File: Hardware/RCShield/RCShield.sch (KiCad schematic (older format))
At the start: 34 parts

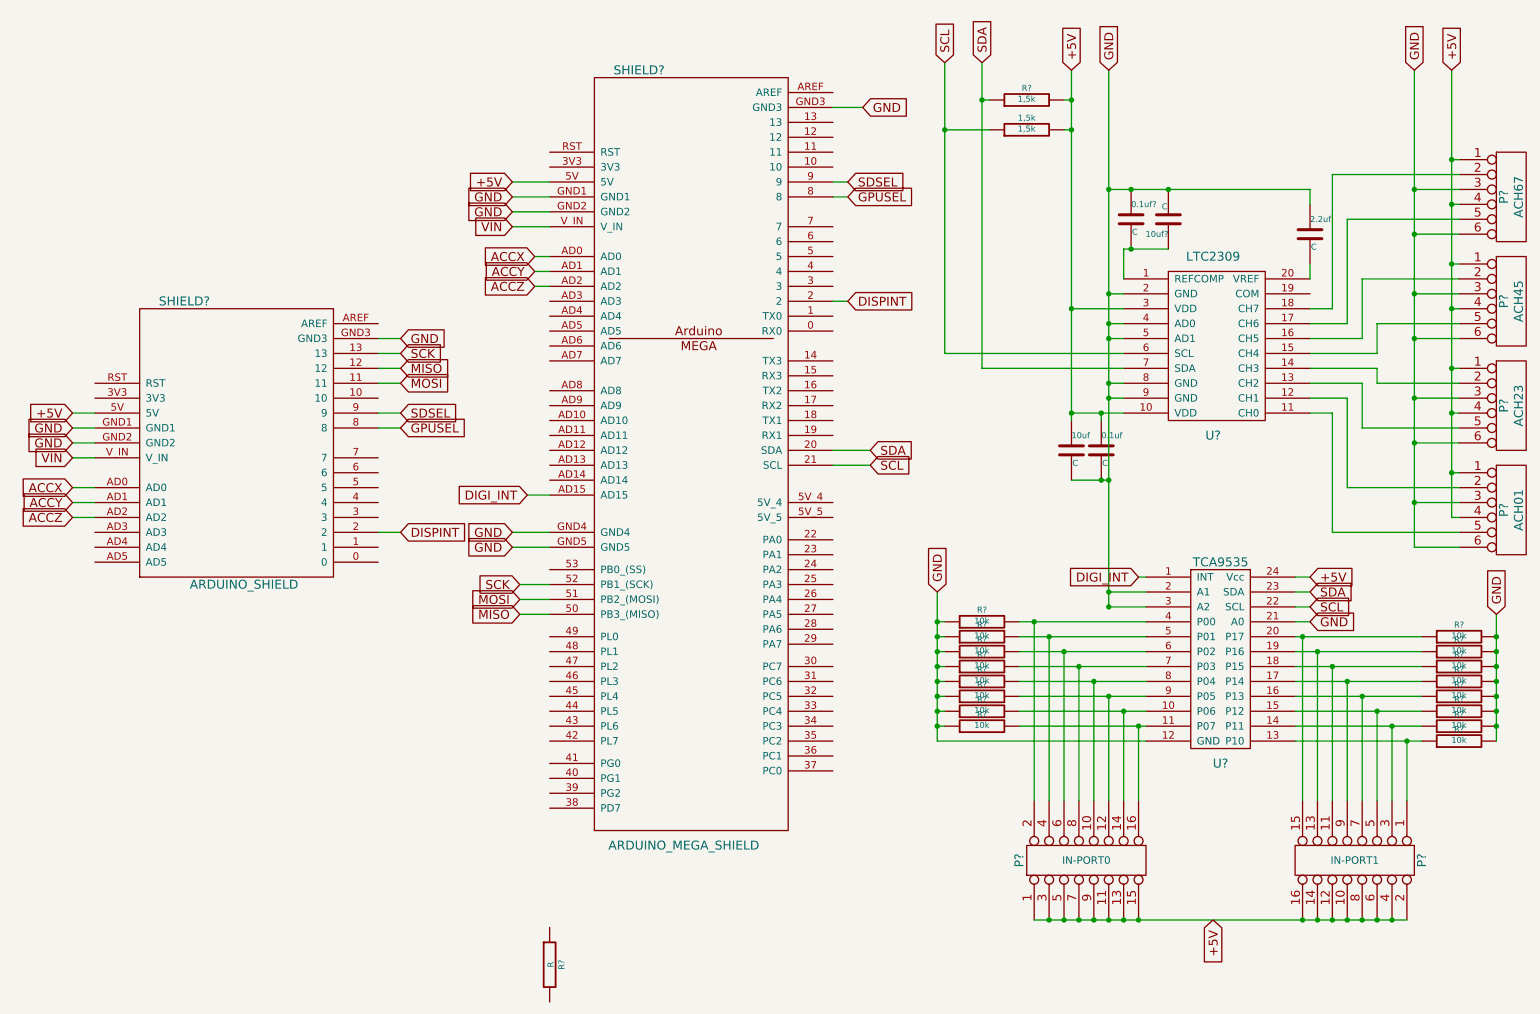
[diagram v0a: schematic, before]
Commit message: Connected I2C Components on the PCB
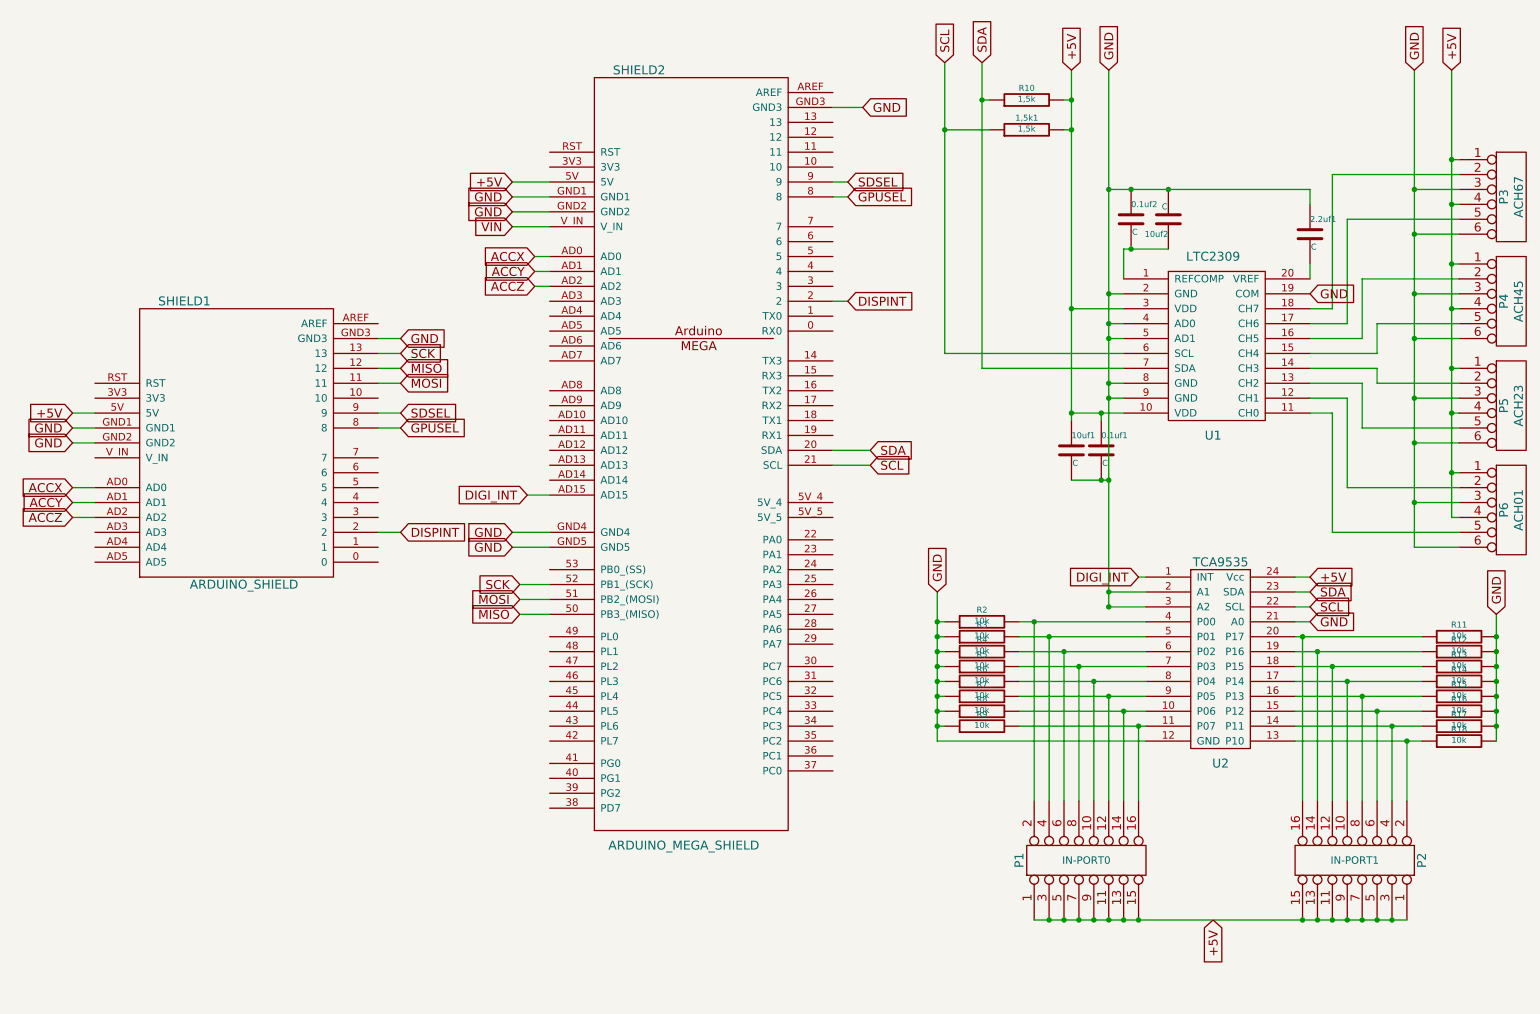
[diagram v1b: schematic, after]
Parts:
- removed R?: R, ~, symbol R
- gave numbers to parts that had none: 29
- renumbered 0.1uf to 0.1uf1, 1,5k to 1,5k1, 10uf to 10uf1, 2.2uf to 2.2uf1
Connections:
- net +5V: now also P2.1, P2.11, P2.13, P2.15, P2.3, P2.5, P2.7, P2.9; no longer P2.10, P2.12, P2.14, P2.16, P2.2, P2.4, P2.6, P2.8
- net GND: now also U1.19 (COM)
- net VIN: no longer SHIELD1.V_IN
- net at R18.1, U2.13 (P10): now also P2.2; no longer P2.1
- net at R17.1, U2.14 (P11): now also P2.4; no longer P2.3
- net at R16.1, U2.15 (P12): now also P2.6; no longer P2.5
- net at R15.1, U2.16 (P13): now also P2.8; no longer P2.7
- net at R14.1, U2.17 (P14): now also P2.10; no longer P2.9
- net at R13.1, U2.18 (P15): now also P2.12; no longer P2.11
- net at R12.1, U2.19 (P16): now also P2.14; no longer P2.13
- net at R11.1, U2.20 (P17): now also P2.16; no longer P2.15
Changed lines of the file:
@@
 Sheet 1 1
 Title ""
-Date "8 may 2014"
+Date "11 may 2014"
 Rev ""
 Comp ""
@@
 $EndDescr
 $Comp
-L ARDUINO_MEGA_SHIELD SHIELD?
+L ARDUINO_MEGA_SHIELD SHIELD2
 U 1 1 536BD2B3
 P 4950 3600
-F 0 "SHIELD?" H 4550 6100 60  0000 C CNN
+F 0 "SHIELD2" H 4550 6100 60  0000 C CNN
 F 1 "ARDUINO_MEGA_SHIELD" H 4850 900 60  0000 C CNN
 F 2 "" H 4950 3600 60  0000 C CNN
@@
 $EndComp
 $Comp
-L LTC2309 U?
+L LTC2309 U1
 U 1 1 536BD2F7
 P 8400 2950
-F 0 "U?" H 8400 2350 60  0000 C CNN
+F 0 "U1" H 8400 2350 60  0000 C CNN
 F 1 "LTC2309" H 8400 3550 60  0000 C CNN
 F 2 "~" H 8400 3550 60  0000 C CNN
@@
 $EndComp
 $Comp
-L TCA9535 U?
+L TCA9535 U2
 U 1 1 536BD306
 P 8450 5050
-F 0 "U?" H 8450 4350 60  0000 C CNN
+F 0 "U2" H 8450 4350 60  0000 C CNN
 F 1 "TCA9535" H 8450 5700 60  0000 C CNN
 F 2 "~" H 8450 5250 60  0000 C CNN
@@
 $EndComp
 $Comp
-L R R?
-U 1 1 536BD35C
-P 3950 7100
-F 0 "R?" V 4030 7100 40  0000 C CNN
-F 1 "R" V 3957 7101 40  0000 C CNN
-F 2 "~" V 3880 7100 30  0000 C CNN
-F 3 "~" H 3950 7100 30  0000 C CNN
-	1    3950 7100
-	1    0    0    -1
-$EndComp
-$Comp
-L C 10uf
+L C 10uf1
 U 1 1 536BD374
 P 7450 3650
-F 0 "10uf" H 7450 3750 40  0000 L CNN
+F 0 "10uf1" H 7450 3750 40  0000 L CNN
 F 1 "C" H 7456 3565 40  0000 L CNN
 F 2 "~" H 7488 3500 30  0000 C CNN
@@
 $EndComp
 $Comp
-L CONN_6 P?
+L CONN_6 P3
 U 1 1 536BD3AD
 P 10400 1950
-F 0 "P?" V 10350 1950 60  0000 C CNN
+F 0 "P3" V 10350 1950 60  0000 C CNN
 F 1 "ACH67" V 10450 1950 60  0000 C CNN
 F 2 "" H 10400 1950 60  0000 C CNN
@@
 $EndComp
 $Comp
-L CONN_6 P?
+L CONN_6 P4
 U 1 1 536BD3BA
 P 10400 2650
-F 0 "P?" V 10350 2650 60  0000 C CNN
+F 0 "P4" V 10350 2650 60  0000 C CNN
 F 1 "ACH45" V 10450 2650 60  0000 C CNN
 F 2 "" H 10400 2650 60  0000 C CNN
@@
 $EndComp
 $Comp
-L CONN_6 P?
+L CONN_6 P5
 U 1 1 536BD3C0
 P 10400 3350
-F 0 "P?" V 10350 3350 60  0000 C CNN
+F 0 "P5" V 10350 3350 60  0000 C CNN
 F 1 "ACH23" V 10450 3350 60  0000 C CNN
 F 2 "" H 10400 3350 60  0000 C CNN
@@
 $EndComp
 $Comp
-L CONN_6 P?
+L CONN_6 P6
 U 1 1 536BD3C8
 P 10400 4050
-F 0 "P?" V 10350 4050 60  0000 C CNN
+F 0 "P6" V 10350 4050 60  0000 C CNN
 F 1 "ACH01" V 10450 4050 60  0000 C CNN
 F 2 "" H 10400 4050 60  0000 C CNN
@@
 +5V
 $Comp
-L R R?
+L R R10
 U 1 1 536BD929
 P 7150 1300
-F 0 "R?" V 7230 1300 40  0000 C CNN
+F 0 "R10" V 7230 1300 40  0000 C CNN
 F 1 "1,5k" V 7157 1301 40  0000 C CNN
 F 2 "~" V 7080 1300 30  0000 C CNN
@@
 SCL
 $Comp
-L R 1,5k
+L R 1,5k1
 U 1 1 536BD948
 P 7150 1500
-F 0 "1,5k" V 7230 1500 40  0000 C CNN
+F 0 "1,5k1" V 7230 1500 40  0000 C CNN
 F 1 "1,5k" V 7157 1501 40  0000 C CNN
 F 2 "~" V 7080 1500 30  0000 C CNN
@@
 +5V
 $Comp
-L R R?
+L R R11
 U 1 1 536BE193
 P 10050 4900
-F 0 "R?" V 10130 4900 40  0000 C CNN
+F 0 "R11" V 10130 4900 40  0000 C CNN
 F 1 "10k" V 10057 4901 40  0000 C CNN
 F 2 "~" V 9980 4900 30  0000 C CNN
@@
 $EndComp
 $Comp
-L R R?
+L R R12
 U 1 1 536BE1BA
 P 10050 5000
-F 0 "R?" V 10130 5000 40  0000 C CNN
+F 0 "R12" V 10130 5000 40  0000 C CNN
 F 1 "10k" V 10057 5001 40  0000 C CNN
 F 2 "~" V 9980 5000 30  0000 C CNN
@@
 $EndComp
 $Comp
-L R R?
+L R R13
 U 1 1 536BE1C0
 P 10050 5100
-F 0 "R?" V 10130 5100 40  0000 C CNN
+F 0 "R13" V 10130 5100 40  0000 C CNN
 F 1 "10k" V 10057 5101 40  0000 C CNN
 F 2 "~" V 9980 5100 30  0000 C CNN
@@
 $EndComp
 $Comp
-L R R?
+L R R14
 U 1 1 536BE1C6
 P 10050 5200
-F 0 "R?" V 10130 5200 40  0000 C CNN
+F 0 "R14" V 10130 5200 40  0000 C CNN
 F 1 "10k" V 10057 5201 40  0000 C CNN
 F 2 "~" V 9980 5200 30  0000 C CNN
@@
 $EndComp
 $Comp
-L R R?
+L R R15
 U 1 1 536BE1CC
 P 10050 5300
-F 0 "R?" V 10130 5300 40  0000 C CNN
+F 0 "R15" V 10130 5300 40  0000 C CNN
 F 1 "10k" V 10057 5301 40  0000 C CNN
 F 2 "~" V 9980 5300 30  0000 C CNN
@@
 $EndComp
 $Comp
-L R R?
+L R R16
 U 1 1 536BE1D2
 P 10050 5400
-F 0 "R?" V 10130 5400 40  0000 C CNN
+F 0 "R16" V 10130 5400 40  0000 C CNN
 F 1 "10k" V 10057 5401 40  0000 C CNN
 F 2 "~" V 9980 5400 30  0000 C CNN
@@
 $EndComp
 $Comp
-L R R?
+L R R17
 U 1 1 536BE1D8
 P 10050 5500
-F 0 "R?" V 10130 5500 40  0000 C CNN
+F 0 "R17" V 10130 5500 40  0000 C CNN
 F 1 "10k" V 10057 5501 40  0000 C CNN
 F 2 "~" V 9980 5500 30  0000 C CNN
@@
 $EndComp
 $Comp
-L R R?
+L R R18
 U 1 1 536BE1DE
 P 10050 5600
-F 0 "R?" V 10130 5600 40  0000 C CNN
+F 0 "R18" V 10130 5600 40  0000 C CNN
 F 1 "10k" V 10057 5601 40  0000 C CNN
 F 2 "~" V 9980 5600 30  0000 C CNN
@@
 $EndComp
 $Comp
-L R R?
+L R R2
 U 1 1 536BE1E4
 P 6850 4800
-F 0 "R?" V 6930 4800 40  0000 C CNN
+F 0 "R2" V 6930 4800 40  0000 C CNN
 F 1 "10k" V 6857 4801 40  0000 C CNN
 F 2 "~" V 6780 4800 30  0000 C CNN
@@
 $EndComp
 $Comp
-L R R?
+L R R3
 U 1 1 536BE1EA
 P 6850 4900
-F 0 "R?" V 6930 4900 40  0000 C CNN
+F 0 "R3" V 6930 4900 40  0000 C CNN
 F 1 "10k" V 6857 4901 40  0000 C CNN
 F 2 "~" V 6780 4900 30  0000 C CNN
@@
 $EndComp
 $Comp
-L R R?
+L R R4
 U 1 1 536BE1F0
 P 6850 5000
-F 0 "R?" V 6930 5000 40  0000 C CNN
+F 0 "R4" V 6930 5000 40  0000 C CNN
 F 1 "10k" V 6857 5001 40  0000 C CNN
 F 2 "~" V 6780 5000 30  0000 C CNN
@@
 $EndComp
 $Comp
-L R R?
+L R R5
 U 1 1 536BE1F6
 P 6850 5100
-F 0 "R?" V 6930 5100 40  0000 C CNN
+F 0 "R5" V 6930 5100 40  0000 C CNN
 F 1 "10k" V 6857 5101 40  0000 C CNN
 F 2 "~" V 6780 5100 30  0000 C CNN
@@
 $EndComp
 $Comp
-L R R?
+L R R6
 U 1 1 536BE1FC
 P 6850 5200
-F 0 "R?" V 6930 5200 40  0000 C CNN
+F 0 "R6" V 6930 5200 40  0000 C CNN
 F 1 "10k" V 6857 5201 40  0000 C CNN
 F 2 "~" V 6780 5200 30  0000 C CNN
@@
 $EndComp
 $Comp
-L R R?
+L R R7
 U 1 1 536BE202
 P 6850 5300
-F 0 "R?" V 6930 5300 40  0000 C CNN
+F 0 "R7" V 6930 5300 40  0000 C CNN
 F 1 "10k" V 6857 5301 40  0000 C CNN
 F 2 "~" V 6780 5300 30  0000 C CNN
@@
 $EndComp
 $Comp
-L R R?
+L R R8
 U 1 1 536BE208
 P 6850 5400
-F 0 "R?" V 6930 5400 40  0000 C CNN
+F 0 "R8" V 6930 5400 40  0000 C CNN
 F 1 "10k" V 6857 5401 40  0000 C CNN
 F 2 "~" V 6780 5400 30  0000 C CNN
@@
 $EndComp
 $Comp
-L R R?
+L R R9
 U 1 1 536BE20E
 P 6850 5500
-F 0 "R?" V 6930 5500 40  0000 C CNN
+F 0 "R9" V 6930 5500 40  0000 C CNN
 F 1 "10k" V 6857 5501 40  0000 C CNN
 F 2 "~" V 6780 5500 30  0000 C CNN
@@
 GND
 $Comp
-L CONN_8X2 P?
+L CONN_8X2 P2
 U 1 1 536BF2CC
 P 9350 6400
-F 0 "P?" H 9350 6850 60  0000 C CNN
+F 0 "P2" H 9350 6850 60  0000 C CNN
 F 1 "IN-PORT1" V 9350 6400 50  0000 C CNN
 F 2 "" H 9350 6400 60  0000 C CNN
 F 3 "" H 9350 6400 60  0000 C CNN
 	1    9350 6400
-	0    1    1    0
-$EndComp
-$Comp
-L CONN_8X2 P?
+	0    1    -1   0
+$EndComp
+$Comp
+L CONN_8X2 P1
 U 1 1 536BF2D9
 P 7550 6400
-F 0 "P?" H 7550 6850 60  0000 C CNN
+F 0 "P1" H 7550 6850 60  0000 C CNN
 F 1 "IN-PORT0" V 7550 6400 50  0000 C CNN
 F 2 "" H 7550 6400 60  0000 C CNN
@@
 +5V
 $Comp
-L ARDUINO_SHIELD SHIELD?
+L ARDUINO_SHIELD SHIELD1
 U 1 1 536C3663
 P 1850 3600
-F 0 "SHIELD?" H 1500 4550 60  0000 C CNN
+F 0 "SHIELD1" H 1500 4550 60  0000 C CNN
 F 1 "ARDUINO_SHIELD" H 1900 2650 60  0000 C CNN
 F 2 "" H 1850 3600 60  0000 C CNN
@@
 Text GLabel 750  3400 0    60   Input ~ 0
 +5V
-Text GLabel 750  3700 0    60   Input ~ 0
-VIN
 Text GLabel 3700 2150 0    60   Input ~ 0
 VIN
 Wire Wire Line
 	3950 2150 3700 2150
-Wire Wire Line
-	750  3700 900  3700
 Wire Wire Line
 	3950 3950 3800 3950
@@
 	750  4100 900  4100
 $Comp
-L C 0.1uf
+L C 0.1uf1
 U 1 1 536C4F0D
 P 7650 3650
-F 0 "0.1uf" H 7650 3750 40  0000 L CNN
+F 0 "0.1uf1" H 7650 3750 40  0000 L CNN
 F 1 "C" H 7656 3565 40  0000 L CNN
 F 2 "~" H 7688 3500 30  0000 C CNN
@@
 Connection ~ 7650 3850
 $Comp
-L C 10uf?
+L C 10uf2
 U 1 1 536C5368
 P 8100 2100
-F 0 "10uf?" H 8100 2200 40  0000 L CNN
+F 0 "10uf2" H 8100 2200 40  0000 L CNN
 F 1 "C" H 8106 2015 40  0000 L CNN
 F 2 "~" H 8138 1950 30  0000 C CNN
@@
 $EndComp
 $Comp
-L C 0.1uf?
+L C 0.1uf2
 U 1 1 536C536E
 P 7850 2100
-F 0 "0.1uf?" H 7850 2200 40  0000 L CNN
+F 0 "0.1uf2" H 7850 2200 40  0000 L CNN
 F 1 "C" H 7856 2015 40  0000 L CNN
 F 2 "~" H 7888 1950 30  0000 C CNN
@@
 Connection ~ 7850 1900
 $Comp
-L C 2.2uf
+L C 2.2uf1
 U 1 1 536C57D4
 P 9050 2200
-F 0 "2.2uf" H 9050 2300 40  0000 L CNN
+F 0 "2.2uf1" H 9050 2300 40  0000 L CNN
 F 1 "C" H 9056 2115 40  0000 L CNN
 F 2 "~" H 9088 2050 30  0000 C CNN
@@
 	9050 1900 9050 2000
 Connection ~ 8100 1900
+Text GLabel 9050 2600 2    60   Input ~ 0
+GND
 $EndSCHEMATC

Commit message: Adding Vsense and PPM Generator Adding PCB File
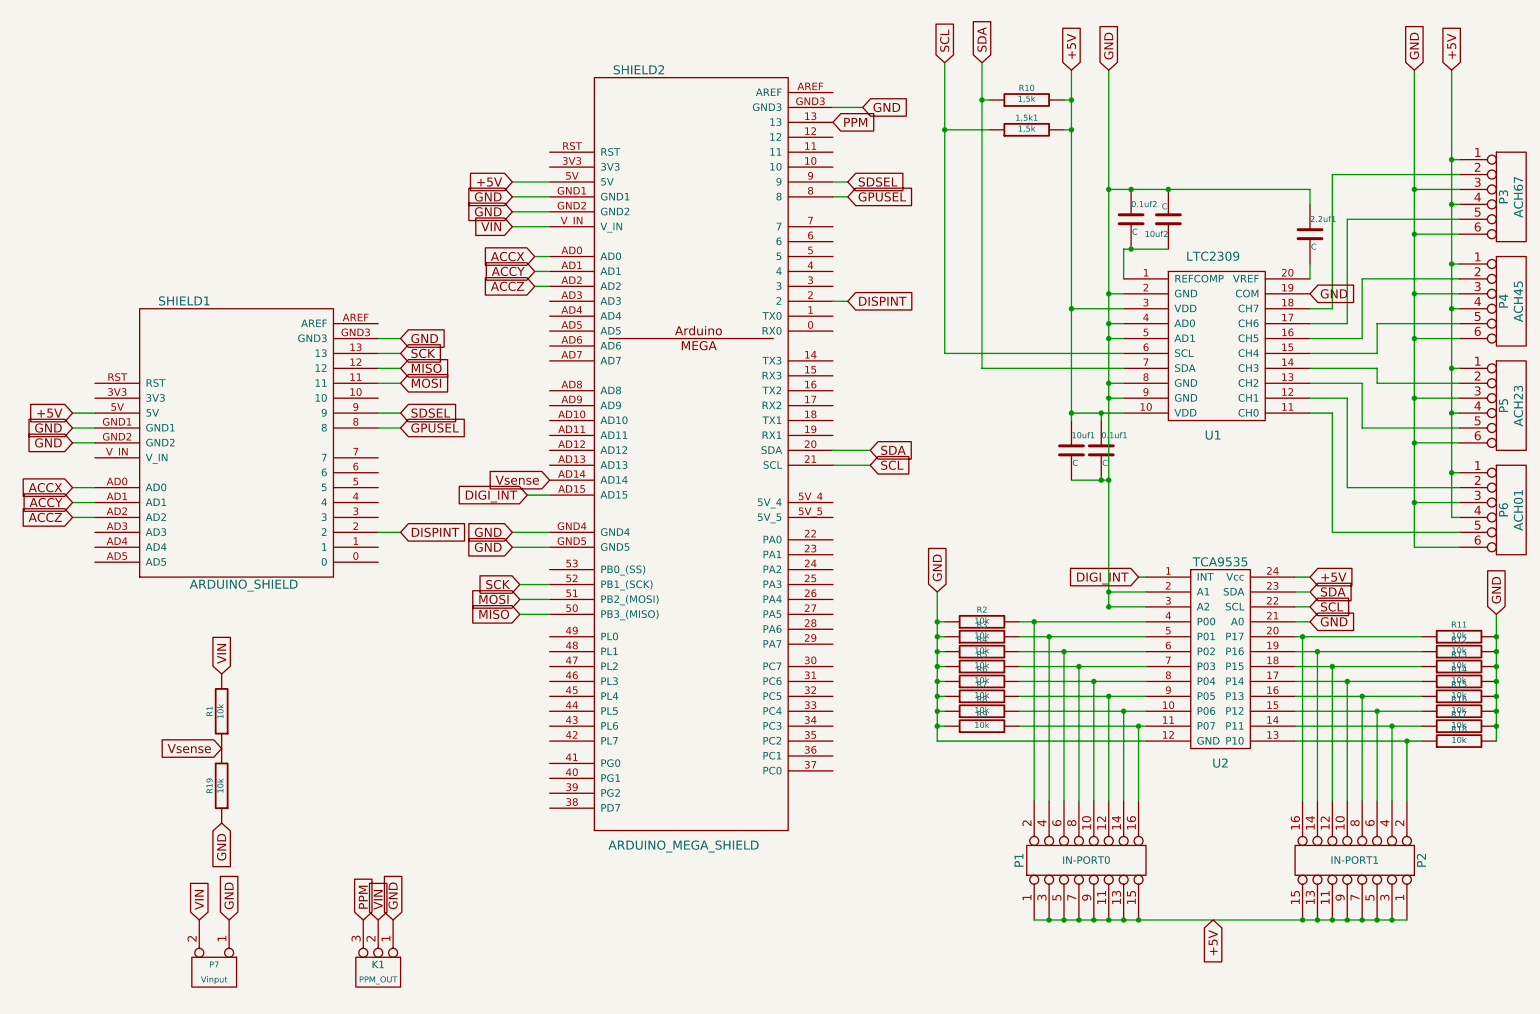
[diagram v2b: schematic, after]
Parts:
- added K1: PPM_OUT, symbol CONN_3
- added P7: Vinput, symbol CONN_2
- added R1, R19: 10k, ~, symbol R
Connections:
- net GND: now also K1.1 (P1), P7.1 (P1), R19.1
- net VIN: now also K1.2 (PM), P7.2 (PM), R1.2
- net PPM: now reaches SHIELD2.13
- net PPM: now also K1.3 (P3)
- net Vsense: now reaches SHIELD2.AD14
- net Vsense: now also R1.1, R19.2
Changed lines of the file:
@@
 Text GLabel 9050 2600 2    60   Input ~ 0
 GND
+$Comp
+L CONN_3 K1
+U 1 1 536F292E
+P 2800 7150
+F 0 "K1" V 2750 7150 50  0000 C CNN
+F 1 "PPM_OUT" V 2850 7150 40  0000 C CNN
+F 2 "" H 2800 7150 60  0000 C CNN
+F 3 "" H 2800 7150 60  0000 C CNN
+	1    2800 7150
+	0    1    1    0
+$EndComp
+Text GLabel 2700 6800 1    60   Input ~ 0
+PPM
+Text GLabel 2800 6800 1    60   Input ~ 0
+VIN
+Text GLabel 2900 6800 1    60   Input ~ 0
+GND
+Text GLabel 5850 1450 2    60   Input ~ 0
+PPM
+$Comp
+L CONN_2 P7
+U 1 1 536F2B46
+P 1700 7150
+F 0 "P7" V 1650 7150 40  0000 C CNN
+F 1 "Vinput" V 1750 7150 40  0000 C CNN
+F 2 "" H 1700 7150 60  0000 C CNN
+F 3 "" H 1700 7150 60  0000 C CNN
+	1    1700 7150
+	0    1    1    0
+$EndComp
+Text GLabel 1800 6800 1    60   Input ~ 0
+GND
+Text GLabel 1600 6800 1    60   Input ~ 0
+VIN
+Text GLabel 3950 3850 0    60   Input ~ 0
+Vsense
+$Comp
+L R R1
+U 1 1 536F2BA6
+P 1750 5400
+F 0 "R1" V 1830 5400 40  0000 C CNN
+F 1 "10k" V 1757 5401 40  0000 C CNN
+F 2 "~" V 1680 5400 30  0000 C CNN
+F 3 "~" H 1750 5400 30  0000 C CNN
+	1    1750 5400
+	-1   0    0    1
+$EndComp
+$Comp
+L R R19
+U 1 1 536F2BAD
+P 1750 5900
+F 0 "R19" V 1830 5900 40  0000 C CNN
+F 1 "10k" V 1757 5901 40  0000 C CNN
+F 2 "~" V 1680 5900 30  0000 C CNN
+F 3 "~" H 1750 5900 30  0000 C CNN
+	1    1750 5900
+	-1   0    0    1
+$EndComp
+Text GLabel 1750 5650 0    60   Input ~ 0
+Vsense
+Text GLabel 1750 6150 3    60   Input ~ 0
+GND
+Text GLabel 1750 5150 1    60   Input ~ 0
+VIN
 $EndSCHEMATC
